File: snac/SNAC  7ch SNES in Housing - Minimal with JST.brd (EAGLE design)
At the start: 79.7 x 64.1 mm, 8 parts, among them U1 PMIC-LDO-XC6206P332MR-G(SOT23), X2 JST-XH-09-PIN-LONG-PAD

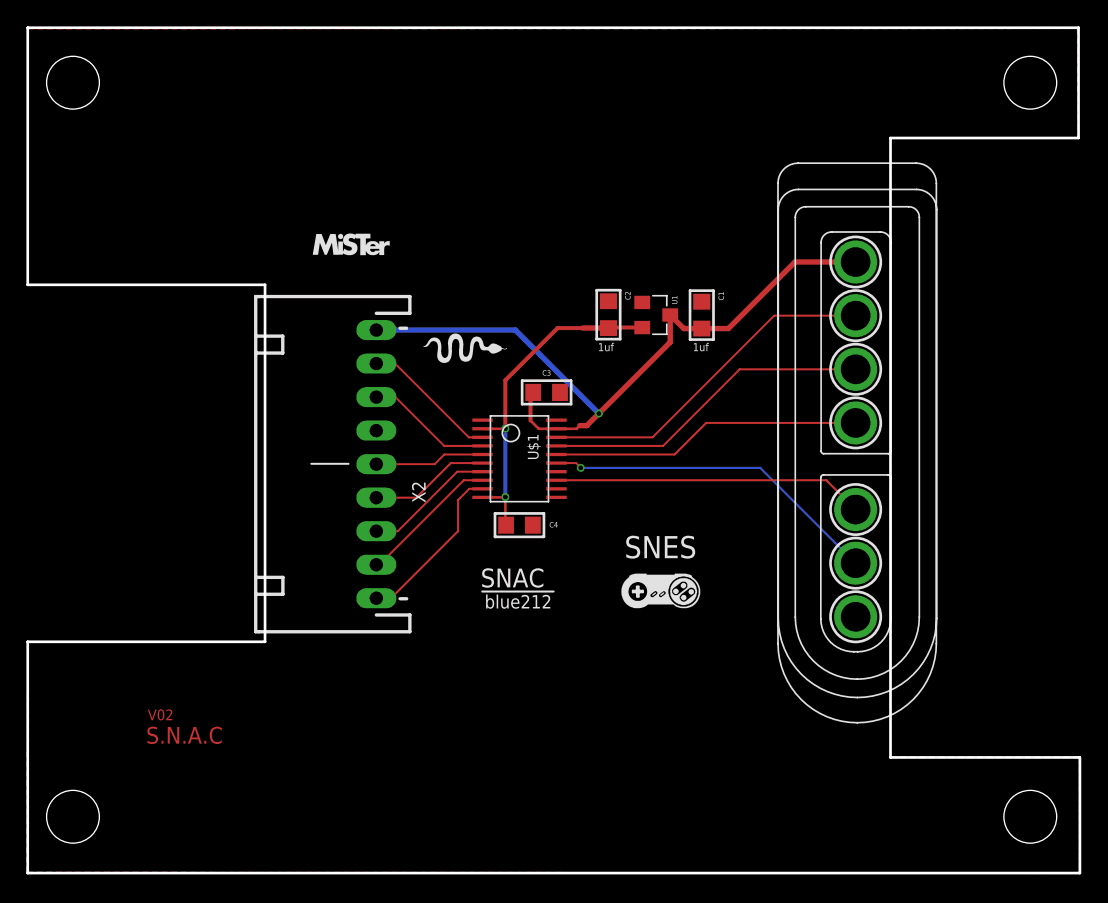
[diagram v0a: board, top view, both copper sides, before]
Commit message: Changed SMS 3D Dongle back to using LV7 on USER IO
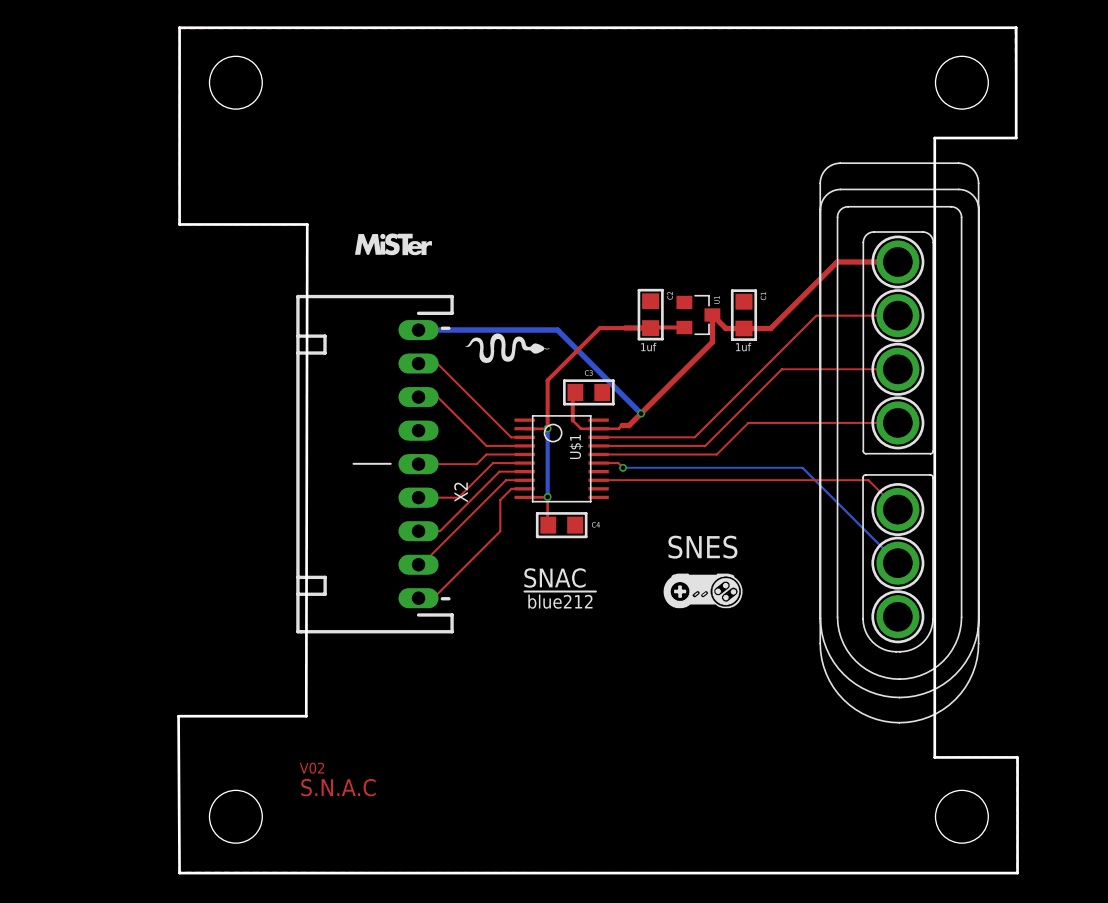
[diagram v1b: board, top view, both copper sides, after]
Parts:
- moved C1 3.20 mm to (55.0, 42.9)
- moved C2 3.20 mm to (48.0, 42.9)
- moved C4 3.20 mm to (41.2, 27.0)
- moved U$1 3.20 mm to (41.2, 32.0)
- moved U$3 3.20 mm to (62.6, 46.9)
- moved U1 3.20 mm to (51.6, 42.9)
- moved X2 3.20 mm to (30.4, 31.6)
- moved C3 3.20 mm to (43.3, 37.0)
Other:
- board size 79.7 x 64.1 mm -> 63.6 x 64.1 mm

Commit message: SMS 3D and SNES SNAC JST updates
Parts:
- moved C1 3.66 mm to (51.4, 42.9)
- moved C2 3.66 mm to (44.3, 42.9)
- moved U1 3.66 mm to (47.9, 42.9)
- moved U$3 3.05 mm to (59.6, 46.9)
- moved C3 0.08 mm to (43.4, 37.0)
- moved C4 0.08 mm to (41.3, 27.0)
- moved U$1 0.08 mm to (41.3, 32.0)
- moved X2 0.08 mm to (30.5, 31.6)
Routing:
- net LV: track 26.5 -> 22.9 mm
- net HV4: track 25.1 -> 22.0 mm
- net HV1: track 23.6 -> 20.5 mm
- net HV6: track 23.7 -> 20.5 mm
- net HV5: track 25.8 -> 22.7 mm
- net HV2: track 26.5 -> 23.4 mm
- net HV: track 54.1 -> 53.2 mm
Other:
- board size 63.6 x 64.1 mm -> 61.3 x 64.2 mm
- board text added: "ElectronAsh"
- board text added: "SNES SNAC+"
- board text removed: "S.N.A.C"
- board text removed: "SNAC"
- board text removed: "SNES"
- board text removed: "V02"

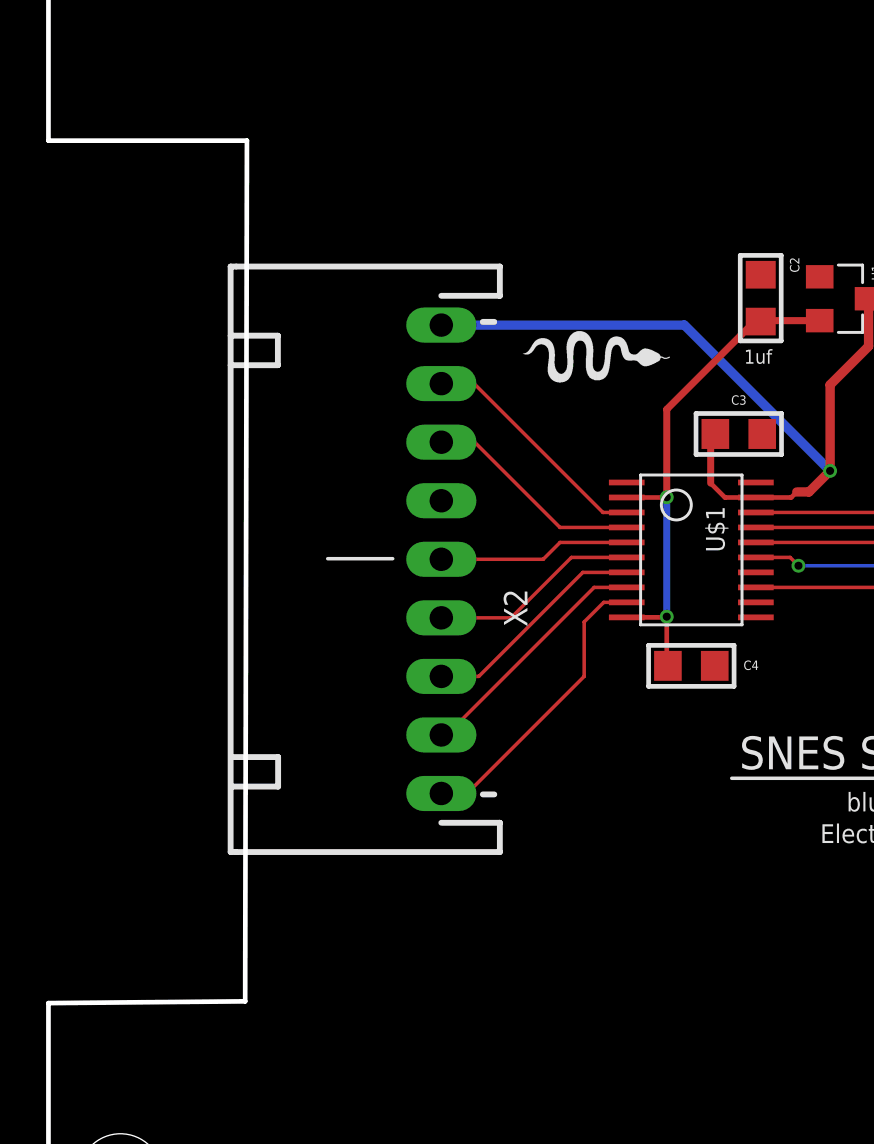
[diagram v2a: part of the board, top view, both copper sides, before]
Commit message: added reversed JST footprint to SNES SNAC Minimal
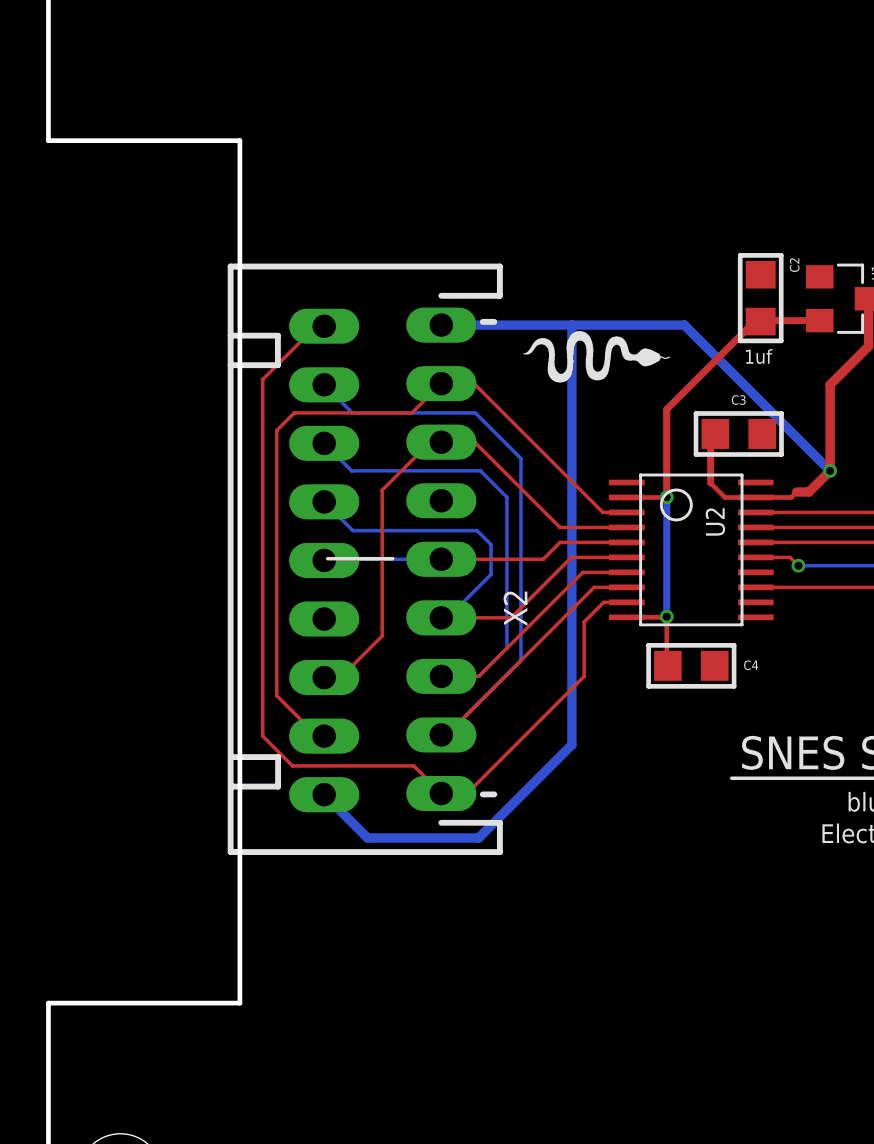
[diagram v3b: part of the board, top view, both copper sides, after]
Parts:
- added X1: JST-XH-09-PIN-LONG-PAD, Rembrandt Electronics - JST XH Connectors v1-0:JST-XH-09-PACKAGE-LONG-PAD
- renumbered U$1 to U2, U$3 to SNES_CON
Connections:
- net GND: now also X1.4
- net HV: now also X1.1
- net LV1: now also X1.8
- net LV2: now also X1.2
- net LV3: now also X1.7
- net LV4: now also X1.3
- net LV5: now also X1.6
- net LV6: now also X1.5
- net LV7: now also X1.9
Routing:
- net HV: track 53.2 -> 84.6 mm
- net LV7: track 12.9 -> 40.7 mm
- net LV1: track 10.7 -> 34.1 mm
- net LV2: track 10.4 -> 32.6 mm
- net LV3: track 9.91 -> 28.7 mm
- net LV4: track 9.58 -> 22.6 mm
- net LV5: track 9.13 -> 21.4 mm
- net LV6: track 8.35 -> 13.4 mm
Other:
- outline, holes or cut-outs redrawn

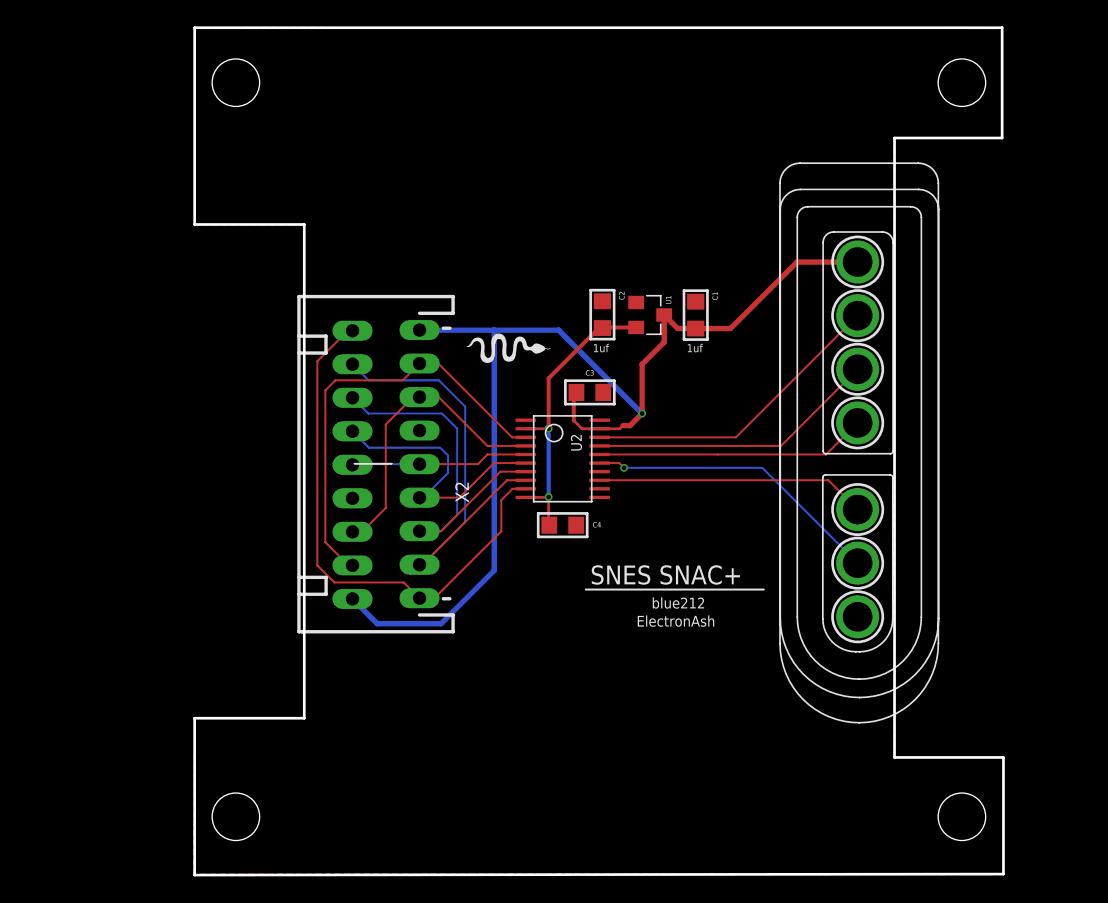
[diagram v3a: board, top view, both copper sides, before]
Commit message: removed the Compact, TXS chip, and SMS3D with USB3 plug versions
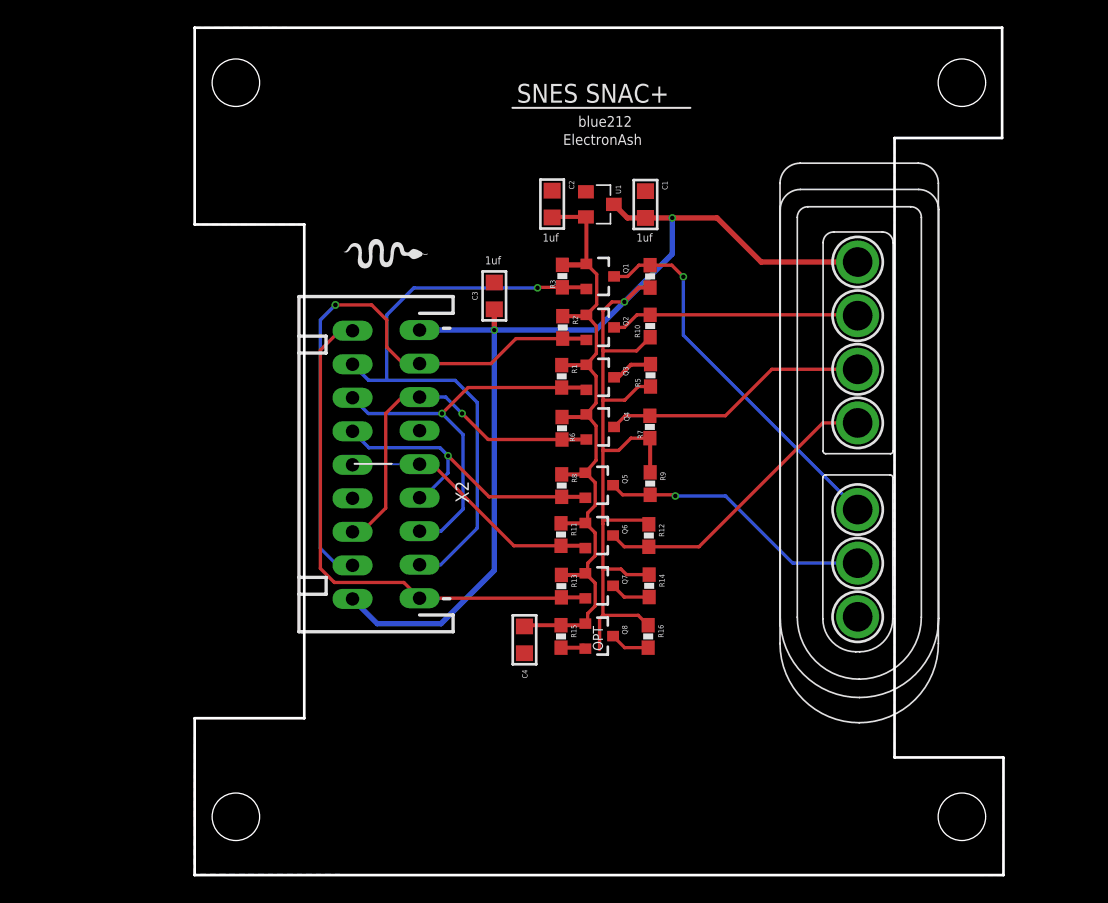
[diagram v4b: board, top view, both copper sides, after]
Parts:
- removed U2: TXS0108, FaBo-LevelTranslator:R-PUSON-N20
- added Q1, Q2, Q3, Q4, Q5, Q6, Q7, Q8: BSS138, SparkFun:SOT23-3
- added R1, R10, R11, R12, R13, R14, R15, R16, R2, R3, R4, R5, R6, R7, R8, R9: 10K, SparkFun:0603-RES
- moved C3 10.3 mm to (36.1, 44.3), turned to 270 degrees
- moved U1 9.21 mm to (44.1, 51.3)
- moved C1 9.21 mm to (47.6, 51.3)
- moved C2 9.21 mm to (40.5, 51.3)
- moved C4 9.16 mm to (38.4, 18.3), turned to 90 degrees
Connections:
- net GND: no longer U2.11
- net HV: now also R10.1, R12.1, R14.1, R16.1, R4.1, R5.1, R7.1, R9.1; no longer U2.19
- net HV1: now also Q1.3, R4.2; no longer U2.13
- net HV2: now also Q2.3, R10.2; no longer U2.18
- net HV3: now also Q3.3, R5.2; no longer U2.14
- net HV4: now also Q4.3, R7.2; no longer U2.17
- net HV5: now also Q5.3, R9.2; no longer U2.15
- net HV6: now also Q6.3, R12.2; no longer U2.16
- net HV7: now also Q7.3, R14.2; no longer U2.12
- net HV8: now also Q8.3, R16.2; no longer U2.20
- net LV: now also Q1.1, Q2.1, Q3.1, Q4.1, Q5.1, Q6.1, Q7.1, Q8.1, R1.1, R11.1, R13.1, R15.1, R2.1, R3.1, R6.1, R8.1; no longer U2.10, U2.2
- net LV1: now also Q1.2, R3.2; no longer U2.8
- net LV2: now also Q2.2, R2.2; no longer U2.3
- net LV3: now also Q3.2, R1.2; no longer U2.7
- net LV4: now also Q4.2, R6.2; no longer U2.4
- net LV5: now also Q5.2, R8.2; no longer U2.6
- net LV6: now also Q6.2, R11.2; no longer U2.5
- net LV7: now also Q7.2, R13.2; no longer U2.9
- net LV8: now also Q8.2, R15.2; no longer U2.1
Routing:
- net HV: track 84.6 -> 133.5 mm, vias 1 -> 3
- net LV: track 22.9 -> 56.4 mm, vias 2 -> 0
- net LV1: track 34.1 -> 46.7 mm, vias 0 -> 1
- net LV2: track 32.6 -> 44.8 mm, vias 0 -> 1
- net HV1: track 20.5 -> 29.2 mm, vias 0 -> 1
- net LV6: track 13.4 -> 20.3 mm
- net LV4: track 22.6 -> 28.0 mm, vias 0 -> 1
- net HV2: track 23.4 -> 18.9 mm
- net HV3: track 0.00 -> 3.26 mm
- net HV7: track 0.00 -> 3.21 mm
- net HV8: track 0.00 -> 3.02 mm
- net LV5: track 21.4 -> 24.0 mm, vias 0 -> 1
- net HV6: track 20.5 -> 22.9 mm
- net LV3: track 28.7 -> 31.0 mm, vias 0 -> 1
- net LV8: track 0.00 -> 2.07 mm
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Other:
- outline, holes or cut-outs redrawn
- board text added: "OPT"
- board text removed: "+"
- board text removed: "-"
